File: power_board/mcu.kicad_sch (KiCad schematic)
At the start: 12 parts, among them U1 STM32L431KCUx

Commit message: Start multichannel layout
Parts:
- added C10: 100n, Capacitor_SMD:C_0603_1608Metric, symbol Device:C_Small
- added R2: 10k, Resistor_SMD:R_0603_1608Metric, symbol Device:R_Small
- C5: renamed from C1; footprint (none) -> Capacitor_SMD:C_0603_1608Metric
- C6: renamed from C2; footprint (none) -> Capacitor_SMD:C_0603_1608Metric
- C7: renamed from C3; footprint (none) -> Capacitor_SMD:C_0603_1608Metric
- C8: renamed from C4; footprint (none) -> Capacitor_SMD:C_0603_1608Metric
- C9: renamed from C5; footprint (none) -> Capacitor_SMD:C_0603_1608Metric
- R1: value 10 -> 1k; footprint (none) -> Resistor_SMD:R_0603_1608Metric
- R3: renamed from R2; footprint (none) -> Resistor_SMD:R_0603_1608Metric
- R4: renamed from R3; footprint (none) -> Resistor_SMD:R_0603_1608Metric
- R5: renamed from R4; footprint (none) -> Resistor_SMD:R_0603_1608Metric
- R6: renamed from R5; footprint (none) -> Resistor_SMD:R_0603_1608Metric
- R7: renamed from R6; footprint (none) -> Resistor_SMD:R_0603_1608Metric
- renumbered U1 to U3
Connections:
- net +3V3: no longer R1.1
- net +3V3A: now also C6.1, C8.1
- net GND: now also C10.1, R2.1
- net at U3.27 (PB4): now also R1.2
- net TELEMETRY: now reaches U3.29 (PB6)
- net TELEMETRY_RX: now reaches U3.30 (PB7)
- net at U3.31 (PH3): now also R2.2
- net at U3.4 (NRST): now also C10.2
- removed net 3V3A: C6.1, C8.1, R1.2
- new net SIGNAL_INPUT: R1.1
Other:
- moved on the sheet: C5, C6, C7, C8, C9, R3, R4, R5, R6, R7, U3

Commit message: Complete primary layout step
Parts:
- renumbered C5 to C1, C6 to C2, C7 to C3, C8 to C4, C9 to C5, C10 to C6, U3 to U1
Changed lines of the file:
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@@
 		(dnp no)
 		(fields_autoplaced yes)
-		(property "Reference" "C8"
+		(property "Reference" "C4"
 			(at 53.34 85.0962 0)
 			(effects
@@
 			(project "power_board"
 				(path "/c786dd1f-c97f-4c1e-a27a-ac5828b3c50c/e75be158-cf9b-4215-a6e9-9f80ecc0638d"
-					(reference "C8")
+					(reference "C4")
 					(unit 1)
 				)
@@
 		(dnp no)
 		(fields_autoplaced yes)
-		(property "Reference" "#PWR012"
+		(property "Reference" "#PWR020"
 			(at 118.11 44.45 0)
 			(effects
@@
 			(project ""
 				(path "/c786dd1f-c97f-4c1e-a27a-ac5828b3c50c/e75be158-cf9b-4215-a6e9-9f80ecc0638d"
-					(reference "#PWR012")
+					(reference "#PWR020")
 					(unit 1)
 				)
@@
 		(dnp no)
 		(fields_autoplaced yes)
-		(property "Reference" "#PWR07"
+		(property "Reference" "#PWR015"
 			(at 39.37 95.25 0)
 			(effects
@@
 			(project "power_board"
 				(path "/c786dd1f-c97f-4c1e-a27a-ac5828b3c50c/e75be158-cf9b-4215-a6e9-9f80ecc0638d"
-					(reference "#PWR07")
+					(reference "#PWR015")
 					(unit 1)
 				)
@@
 		(dnp no)
 		(fields_autoplaced yes)
-		(property "Reference" "#PWR06"
+		(property "Reference" "#PWR014"
 			(at 39.37 81.28 0)
 			(effects
@@
 			(project "power_board"
 				(path "/c786dd1f-c97f-4c1e-a27a-ac5828b3c50c/e75be158-cf9b-4215-a6e9-9f80ecc0638d"
-					(reference "#PWR06")
+					(reference "#PWR014")
 					(unit 1)
 				)
@@
 		(dnp no)
 		(fields_autoplaced yes)
-		(property "Reference" "#PWR013"
+		(property "Reference" "#PWR021"
 			(at 120.65 106.68 0)
 			(effects
@@
 			(project "power_board"
 				(path "/c786dd1f-c97f-4c1e-a27a-ac5828b3c50c/e75be158-cf9b-4215-a6e9-9f80ecc0638d"
-					(reference "#PWR013")
+					(reference "#PWR021")
 					(unit 1)
 				)
@@
 		(dnp no)
 		(fields_autoplaced yes)
-		(property "Reference" "C7"
+		(property "Reference" "C3"
 			(at 52.07 45.7262 0)
 			(effects
@@
 			(project "power_board"
 				(path "/c786dd1f-c97f-4c1e-a27a-ac5828b3c50c/e75be158-cf9b-4215-a6e9-9f80ecc0638d"
-					(reference "C7")
+					(reference "C3")
 					(unit 1)
 				)
@@
 		(dnp no)
 		(fields_autoplaced yes)
-		(property "Reference" "#PWR09"
+		(property "Reference" "#PWR017"
 			(at 96.52 66.04 0)
 			(effects
@@
 			(project "power_board"
 				(path "/c786dd1f-c97f-4c1e-a27a-ac5828b3c50c/e75be158-cf9b-4215-a6e9-9f80ecc0638d"
-					(reference "#PWR09")
+					(reference "#PWR017")
 					(unit 1)
 				)
@@
 		(dnp no)
 		(fields_autoplaced yes)
-		(property "Reference" "#PWR011"
+		(property "Reference" "#PWR019"
 			(at 109.22 106.68 0)
 			(effects
@@
 			(project "power_board"
 				(path "/c786dd1f-c97f-4c1e-a27a-ac5828b3c50c/e75be158-cf9b-4215-a6e9-9f80ecc0638d"
-					(reference "#PWR011")
+					(reference "#PWR019")
 					(unit 1)
 				)
@@
 		(dnp no)
 		(fields_autoplaced yes)
-		(property "Reference" "#PWR010"
+		(property "Reference" "#PWR018"
 			(at 96.52 50.8 0)
 			(effects
@@
 			(project "power_board"
 				(path "/c786dd1f-c97f-4c1e-a27a-ac5828b3c50c/e75be158-cf9b-4215-a6e9-9f80ecc0638d"
-					(reference "#PWR010")
+					(reference "#PWR018")
 					(unit 1)
 				)
@@
 		(dnp no)
 		(fields_autoplaced yes)
-		(property "Reference" "#PWR016"
+		(property "Reference" "#PWR024"
 			(at 182.88 95.25 0)
 			(effects
@@
 			(project "power_board"
 				(path "/c786dd1f-c97f-4c1e-a27a-ac5828b3c50c/e75be158-cf9b-4215-a6e9-9f80ecc0638d"
-					(reference "#PWR016")
+					(reference "#PWR024")
 					(unit 1)
 				)
@@
 		(dnp no)
 		(fields_autoplaced yes)
-		(property "Reference" "#PWR05"
+		(property "Reference" "#PWR013"
 			(at 39.37 59.69 0)
 			(effects
@@
 			(project "power_board"
 				(path "/c786dd1f-c97f-4c1e-a27a-ac5828b3c50c/e75be158-cf9b-4215-a6e9-9f80ecc0638d"
-					(reference "#PWR05")
+					(reference "#PWR013")
 					(unit 1)
 				)
@@
 		(dnp no)
 		(fields_autoplaced yes)
-		(property "Reference" "#PWR04"
+		(property "Reference" "#PWR012"
 			(at 39.37 46.99 0)
 			(effects
@@
 			(project "power_board"
 				(path "/c786dd1f-c97f-4c1e-a27a-ac5828b3c50c/e75be158-cf9b-4215-a6e9-9f80ecc0638d"
-					(reference "#PWR04")
+					(reference "#PWR012")
 					(unit 1)
 				)
@@
 		(dnp no)
 		(fields_autoplaced yes)
-		(property "Reference" "C5"
+		(property "Reference" "C1"
 			(at 41.91 45.7262 0)
 			(effects
@@
 			(project ""
 				(path "/c786dd1f-c97f-4c1e-a27a-ac5828b3c50c/e75be158-cf9b-4215-a6e9-9f80ecc0638d"
-					(reference "C5")
+					(reference "C1")
 					(unit 1)
 				)
@@
 		(dnp no)
 		(fields_autoplaced yes)
-		(property "Reference" "C10"
+		(property "Reference" "C6"
 			(at 105.4163 44.45 90)
 			(effects
@@
 			(project ""
 				(path "/c786dd1f-c97f-4c1e-a27a-ac5828b3c50c/e75be158-cf9b-4215-a6e9-9f80ecc0638d"
-					(reference "C10")
+					(reference "C6")
 					(unit 1)
 				)
@@
 		(dnp no)
 		(fields_autoplaced yes)
-		(property "Reference" "#PWR015"
+		(property "Reference" "#PWR023"
 			(at 182.88 76.2 0)
 			(effects
@@
 			(project ""
 				(path "/c786dd1f-c97f-4c1e-a27a-ac5828b3c50c/e75be158-cf9b-4215-a6e9-9f80ecc0638d"
-					(reference "#PWR015")
+					(reference "#PWR023")
 					(unit 1)
 				)
@@
 		(dnp no)
 		(fields_autoplaced yes)
-		(property "Reference" "C6"
+		(property "Reference" "C2"
 			(at 41.91 85.0962 0)
 			(effects
@@
 			(project "power_board"
 				(path "/c786dd1f-c97f-4c1e-a27a-ac5828b3c50c/e75be158-cf9b-4215-a6e9-9f80ecc0638d"
-					(reference "C6")
+					(reference "C2")
 					(unit 1)
 				)
@@
 		(dnp no)
 		(fields_autoplaced yes)
-		(property "Reference" "#PWR014"
+		(property "Reference" "#PWR022"
 			(at 123.19 44.45 0)
 			(effects
@@
 			(project "power_board"
 				(path "/c786dd1f-c97f-4c1e-a27a-ac5828b3c50c/e75be158-cf9b-4215-a6e9-9f80ecc0638d"
-					(reference "#PWR014")
+					(reference "#PWR022")
 					(unit 1)
 				)
@@
 		(dnp no)
 		(fields_autoplaced yes)
-		(property "Reference" "U3"
+		(property "Reference" "U1"
 			(at 122.7933 96.52 0)
 			(effects
@@
 			(project "power_board"
 				(path "/c786dd1f-c97f-4c1e-a27a-ac5828b3c50c/e75be158-cf9b-4215-a6e9-9f80ecc0638d"
-					(reference "U3")
+					(reference "U1")
 					(unit 1)
 				)
@@
 		(dnp no)
 		(fields_autoplaced yes)
-		(property "Reference" "#PWR08"
+		(property "Reference" "#PWR016"
 			(at 50.8 95.25 0)
 			(effects
@@
 			(project "power_board"
 				(path "/c786dd1f-c97f-4c1e-a27a-ac5828b3c50c/e75be158-cf9b-4215-a6e9-9f80ecc0638d"
-					(reference "#PWR08")
+					(reference "#PWR016")
 					(unit 1)
 				)
@@
 		(dnp no)
 		(fields_autoplaced yes)
-		(property "Reference" "C9"
+		(property "Reference" "C5"
 			(at 60.96 45.7262 0)
 			(effects
@@
 			(project "power_board"
 				(path "/c786dd1f-c97f-4c1e-a27a-ac5828b3c50c/e75be158-cf9b-4215-a6e9-9f80ecc0638d"
-					(reference "C9")
-					(unit 1)
-				)
+					(reference "C5")
+					(unit 1)
+				)

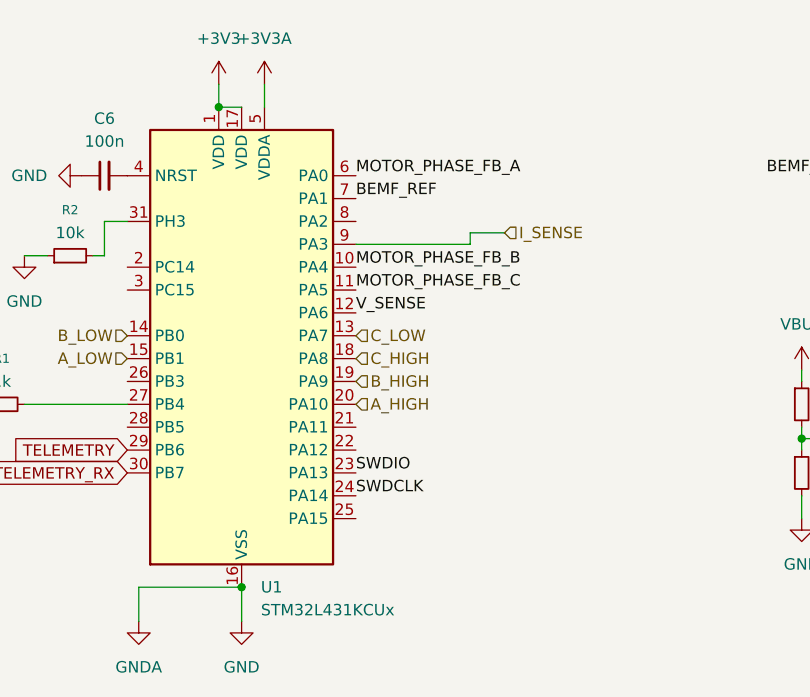
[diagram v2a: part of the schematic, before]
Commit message: Complete layout, and copper zone design
TODO!!!: move DCDC zone from GND area to PGND(current+)
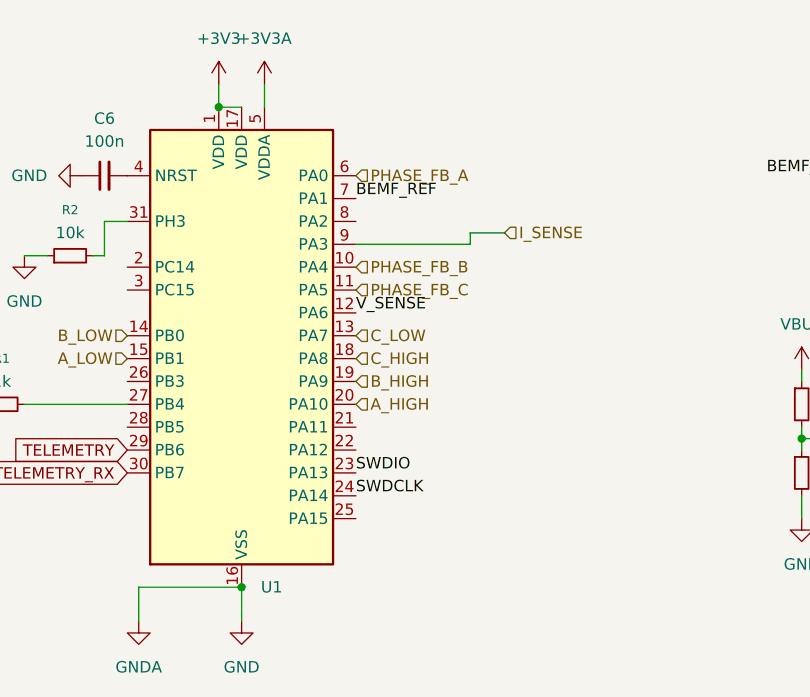
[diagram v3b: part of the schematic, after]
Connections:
- net MOTOR_PHASE_FB_A is gone; now on net PHASE_FB_A : U1.6 (PA0)
- net MOTOR_PHASE_FB_B is gone; now on net PHASE_FB_B: U1.10 (PA4)
- net MOTOR_PHASE_FB_C is gone; now on net PHASE_FB_C: U1.11 (PA5)
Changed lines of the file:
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@@
-		)
-	)
-	(label "MOTOR_PHASE_FB_A"
-		(at 133.35 50.8 0)
-		(effects
-			(font
-				(size 1.27 1.27)
-			)
-			(justify left bottom)
 		)
 	)
@@
 		)
 	)
-	(label "MOTOR_PHASE_FB_C"
-		(at 133.35 63.5 0)
-		(effects
-			(font
-				(size 1.27 1.27)
-			)
-			(justify left bottom)
-		)
-	)
 	(label "BEMF_A"
 		(at -27.94 41.91 180)
@@
 	(label "BEMF_REF"
 		(at -34.29 59.69 0)
-		(effects
-			(font
-				(size 1.27 1.27)
-			)
-			(justify left bottom)
-		)
-	)
-	(label "MOTOR_PHASE_FB_B"
-		(at 133.35 60.96 0)
 		(effects
 			(font
@@
 		)
 	)
+	(hierarchical_label "PHASE_FB_A "
+		(shape input)
+		(at 133.35 50.8 0)
+		(effects
+			(font
+				(size 1.27 1.27)
+			)
+			(justify left)
+		)
+	)
 	(hierarchical_label "B_LOW"
 		(shape input)
@@
 		)
 	)
+	(hierarchical_label "PHASE_FB_C"
+		(shape input)
+		(at 133.35 63.5 0)
+		(effects
+			(font
+				(size 1.27 1.27)
+			)
+			(justify left)
+		)
+	)
 	(hierarchical_label "B_HIGH"
 		(shape input)
@@
 		)
 	)
+	(hierarchical_label "PHASE_FB_B"
+		(shape input)
+		(at 133.35 60.96 0)
+		(effects
+			(font
+				(size 1.27 1.27)
+			)
+			(justify left)
+		)
+	)
 	(hierarchical_label "PHASE_FB_A "
 		(shape input)
@@
 				)
 				(justify left)
-			)
-		)
+				(hide yes)
+			)
+		)

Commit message: All drc error solved
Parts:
- added J1: Conn_ARM_SWD_TagConnect_TC2030-NL, Connector:Tag-Connect_TC2030-IDC-NL_2x03_P1.27mm_Vertical, symbol Connector:Conn_ARM_SWD_TagConnect_TC2030-NL
- U1: footprint Package_DFN_QFN:QFN-32-1EP_5x5mm_P0.5mm_EP3.1x3.1mm_ThermalVias -> Package_DFN_QFN:QFN-32-1EP_5x5mm_P0.5mm_EP3.1x3.1mm
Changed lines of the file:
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@@
+	)
+	(symbol
+		(lib_id "Connector:Conn_ARM_SWD_TagConnect_TC2030-NL")
+		(at 44.45 134.62 0)
+		(unit 1)
+		(exclude_from_sim no)
+		(in_bom no)
+		(on_board yes)
+		(dnp no)
+		(property "Reference" "J1"
+			(at 38.1 133.3499 0)
+			(effects
+				(font
+					(size 1.27 1.27)
+				)
+				(justify right)
+			)
+		)
+		(property "Value" "Conn_ARM_SWD_TagConnect_TC2030-NL"
+			(at 69.088 151.13 0)
+			(effects
+				(font
+					(size 1.27 1.27)
+				)
+				(justify right)
+			)
+		)
+		(property "Footprint" "Connector:Tag-Connect_TC2030-IDC-NL_2x03_P1.27mm_Vertical"
+			(at 44.45 152.4 0)
+			(effects
+				(font
+					(size 1.27 1.27)
+				)
+				(hide yes)
+			)
+		)
+		(property "Datasheet" "https://www.tag-connect.com/wp-content/uploads/bsk-pdf-manager/TC2030-CTX_1.pdf"
+			(at 44.45 149.86 0)
+			(effects
+				(font
+					(size 1.27 1.27)
+				)
+				(hide yes)
+			)
+		)
+		(property "Description" "Tag-Connect ARM Cortex SWD JTAG connector, 6 pin, no legs"
+			(at 44.45 134.62 0)
+			(effects
+				(font
+					(size 1.27 1.27)
+				)
+				(hide yes)
+			)
+		)
+		(pin "1"
+		)
+		(pin "5"
+		)
+		(pin "3"
+		)
+		(pin "4"
+		)
+		(pin "2"
+		)
+		(pin "6"
+		)
+		(instances
+			(project ""
+				(path "/c786dd1f-c97f-4c1e-a27a-ac5828b3c50c/e75be158-cf9b-4215-a6e9-9f80ecc0638d"
+					(reference "J1")
+					(unit 1)
+				)
+			)
+		)
 	)
 	(symbol
@@
 			)
 		)
-		(property "Footprint" "Package_DFN_QFN:QFN-32-1EP_5x5mm_P0.5mm_EP3.1x3.1mm_ThermalVias"
+		(property "Footprint" "Package_DFN_QFN:QFN-32-1EP_5x5mm_P0.5mm_EP3.1x3.1mm"
 			(at 110.49 93.98 0)
 			(effects

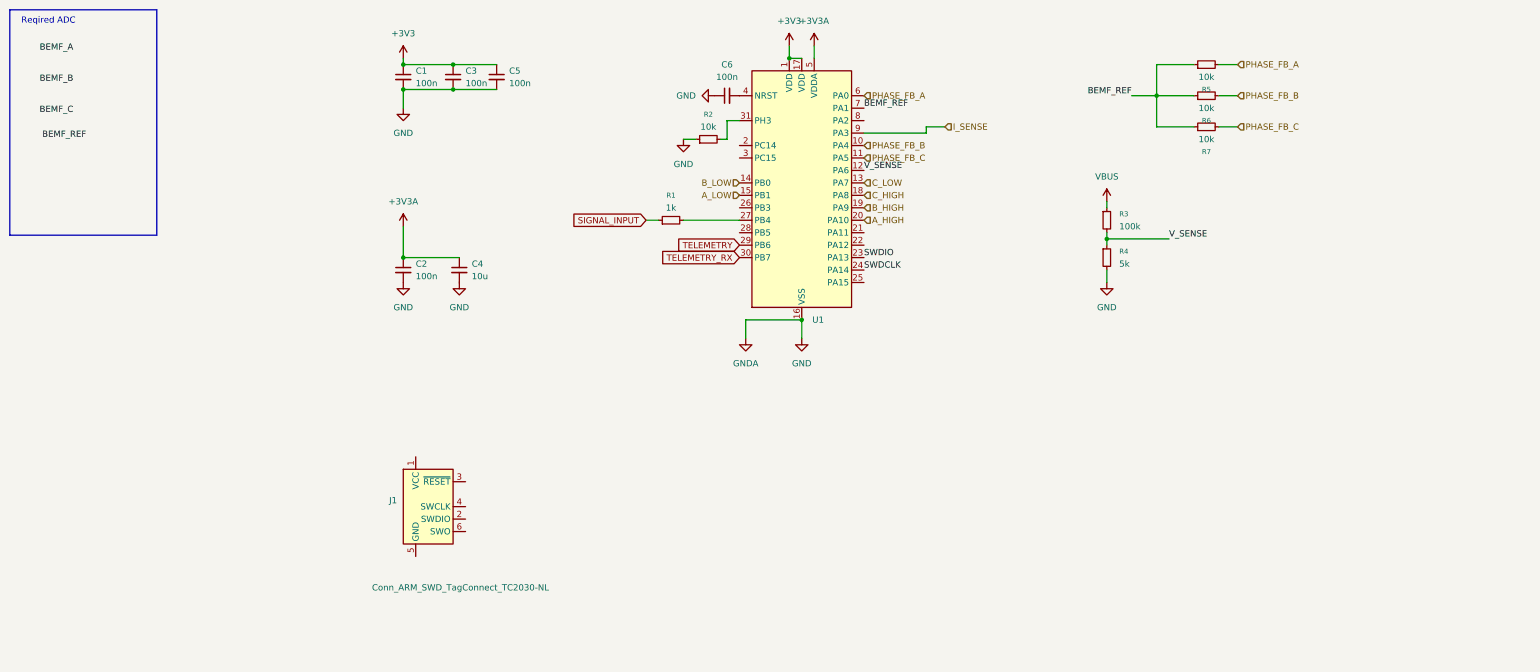
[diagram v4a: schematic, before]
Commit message: Add testpoint, SWD, and PWM port
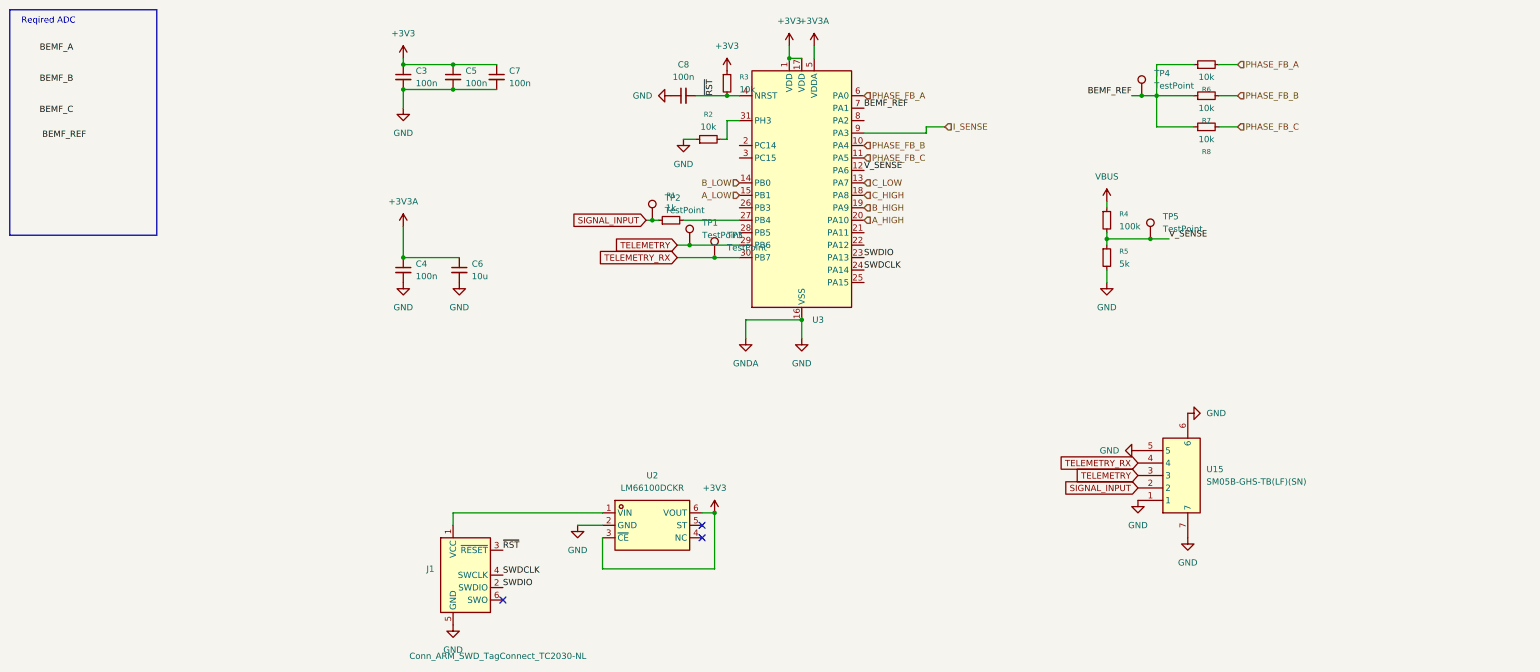
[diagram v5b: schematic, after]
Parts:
- added R3: 10k, Resistor_SMD:R_0603_1608Metric, symbol Device:R_Small
- added TP1, TP2, TP3, TP4, TP5: TestPoint, esc-library:SMD_RH-5015, symbol Connector:TestPoint
- added U15: SM05B-GHS-TB(LF)(SN), esc-library:CONN-SMD_5P-P1.25_SM05B-GHS-TB-LF-SN, symbol esc-library:SM05B-GHS-TB(LF)(SN)
- added U2: LM66100DCKR, esc-library:SC-70-6_L2.0-W1.3-P0.65-LS2.1-BL, symbol esc-library:LM66100DCKR
- renumbered C1 to C3, C2 to C4, C3 to C5, C4 to C6, C5 to C7, C6 to C8, R3 to R4, R4 to R5, R5 to R6, R6 to R7, R7 to R8, U1 to U3
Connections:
- net +3V3: now also R3.1, U2.3 (~{CE}), U2.6 (VOUT)
- net BEMF_REF: now also TP4.1
- net GND: now also J1.5 (GND), U15.1, U15.5, U15.6, U15.7, U2.2 (GND)
- net SIGNAL_INPUT: now also TP2.1, U15.2
- net SWDCLK: now also J1.4 (SWCLK)
- net SWDIO: now also J1.2 (SWDIO)
- net TELEMETRY: now also TP1.1, U15.3
- net TELEMETRY_RX: now also TP3.1, U15.4
- net V_SENSE: now also TP5.1
- net at J1.1 (VCC): now also U2.1 (VIN)
- net ~{RST}: now reaches J1.3 (~{RESET})
- net ~{RST}: now also C8.2, U3.4 (NRST), R3.2
- no-connect marks 0 -> 3
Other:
- moved on the sheet: C8, J1

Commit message: Complete all design, pass DRC
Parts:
- added TP36: GND, esc-library:SMD_RH-5015, symbol Connector:TestPoint
- added U16: SM05B-GHS-TB(LF)(SN), esc-library:CONN-SMD_5P-P1.25_SM05B-GHS-TB-LF-SN, symbol esc-library:SM05B-GHS-TB(LF)(SN)
- TP1: value TestPoint -> TELE
- TP2: value TestPoint -> SIG_IN
- TP3: value TestPoint -> TELE_RX
- TP4: value TestPoint -> BEMF_REF
- TP5: value TestPoint -> VBUS_SENSE
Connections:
- net GND: now also TP36.1, U16.1, U16.6, U16.7
- net SWDCLK: now also U16.3
- net SWDIO: now also U16.2
- net ~{RST}: now also U16.4
- net +3V3SWD: now reaches J1.1 (VCC), U2.1 (VIN)
- net +3V3SWD: now also U16.5
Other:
- moved on the sheet: J1, TP5, U15, U2
